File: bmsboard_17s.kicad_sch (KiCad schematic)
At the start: 0 parts

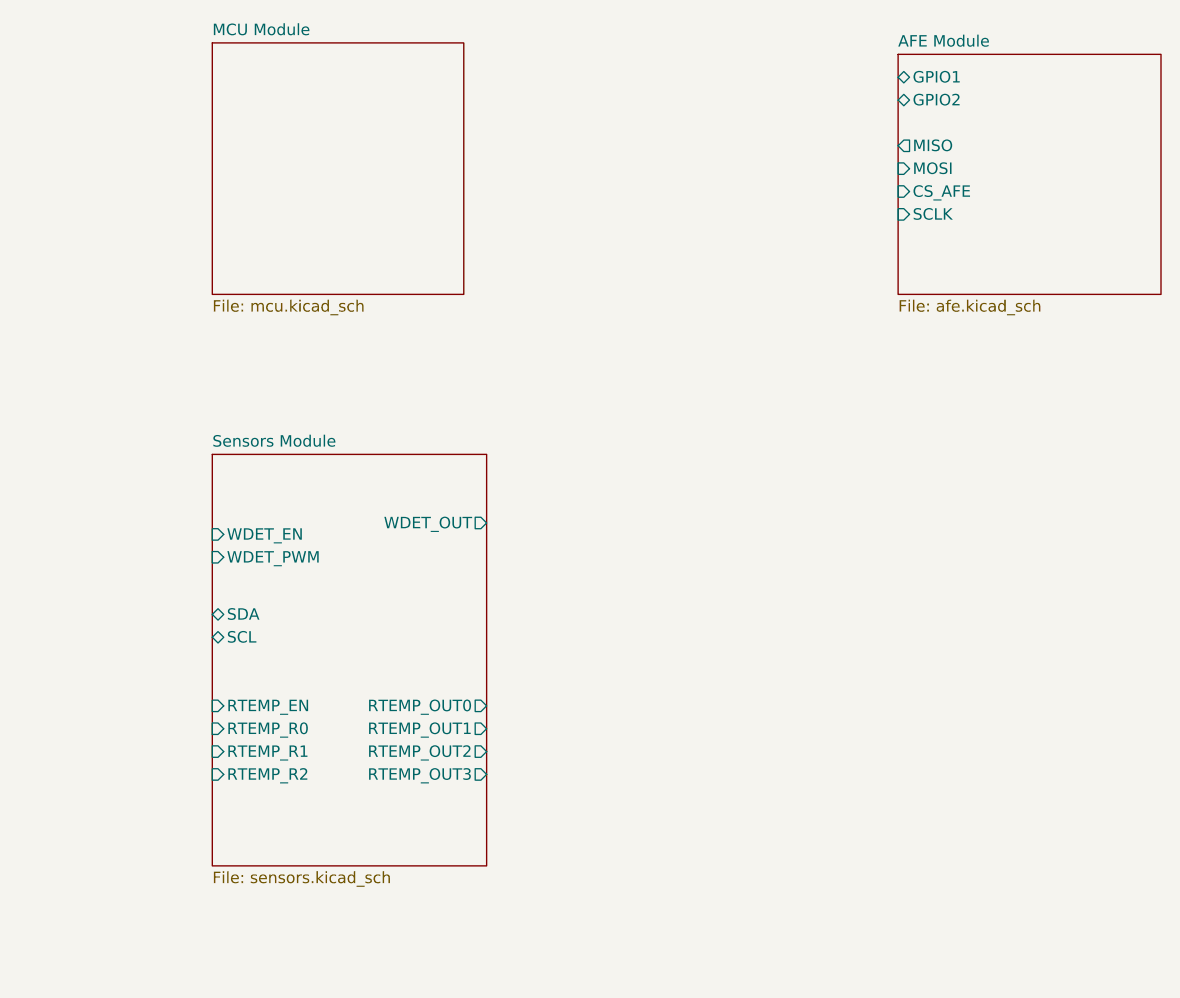
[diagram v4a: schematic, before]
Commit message: 分配MCU引脚，连接原理图，添加CAN收发器
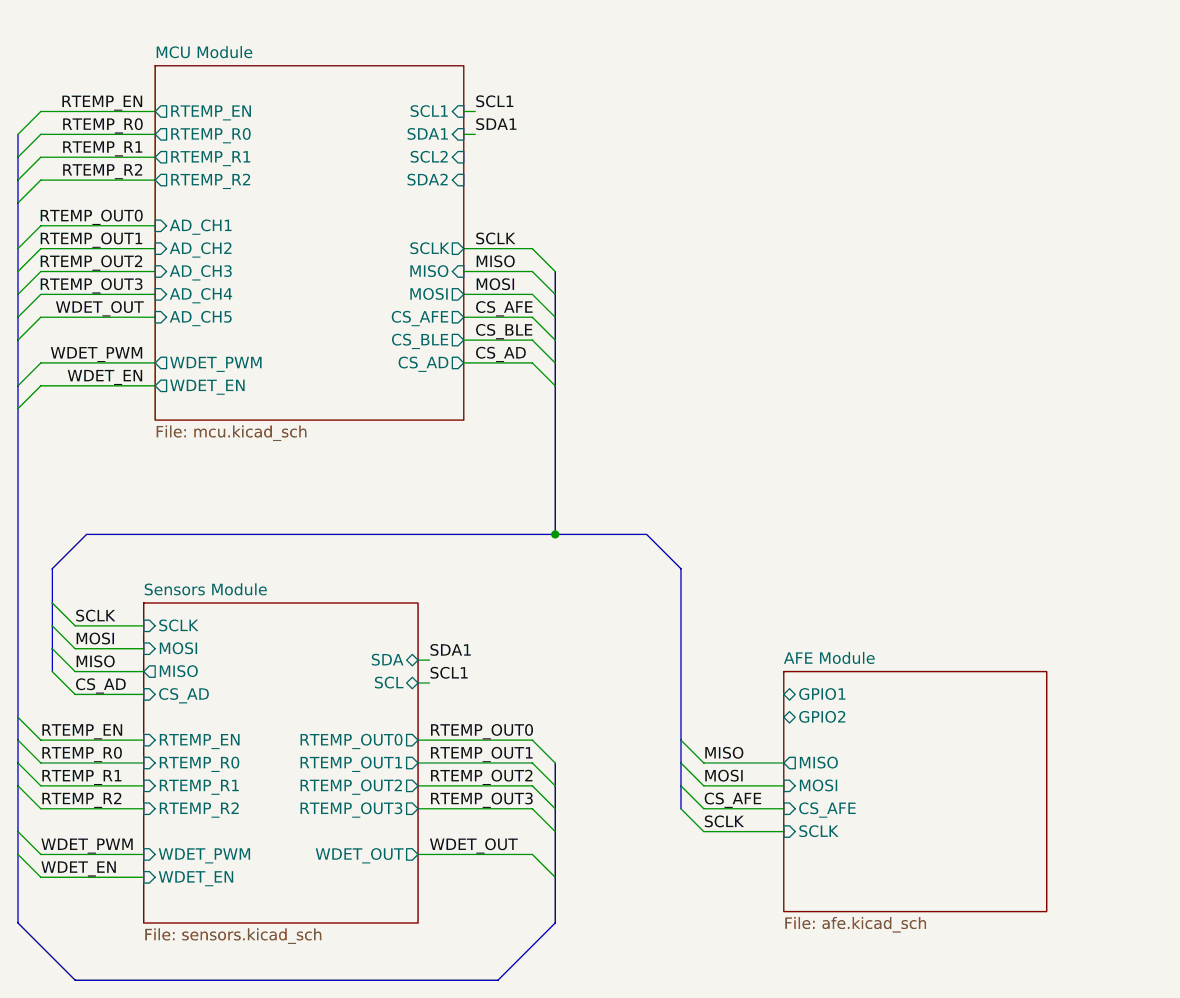
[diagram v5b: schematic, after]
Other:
- sheet MCU Module ports: added AD_CH1, AD_CH2, AD_CH3, AD_CH4, AD_CH5, CS_AD, CS_AFE, CS_BLE, MISO, MOSI, RTEMP_EN, RTEMP_R0, RTEMP_R1, RTEMP_R2, SCL1, SCL2, SCLK, SDA1, SDA2, WDET_EN, WDET_PWM; removed none
- sheet Sensors Module ports: added CS_AD, MISO, MOSI, SCLK; removed none

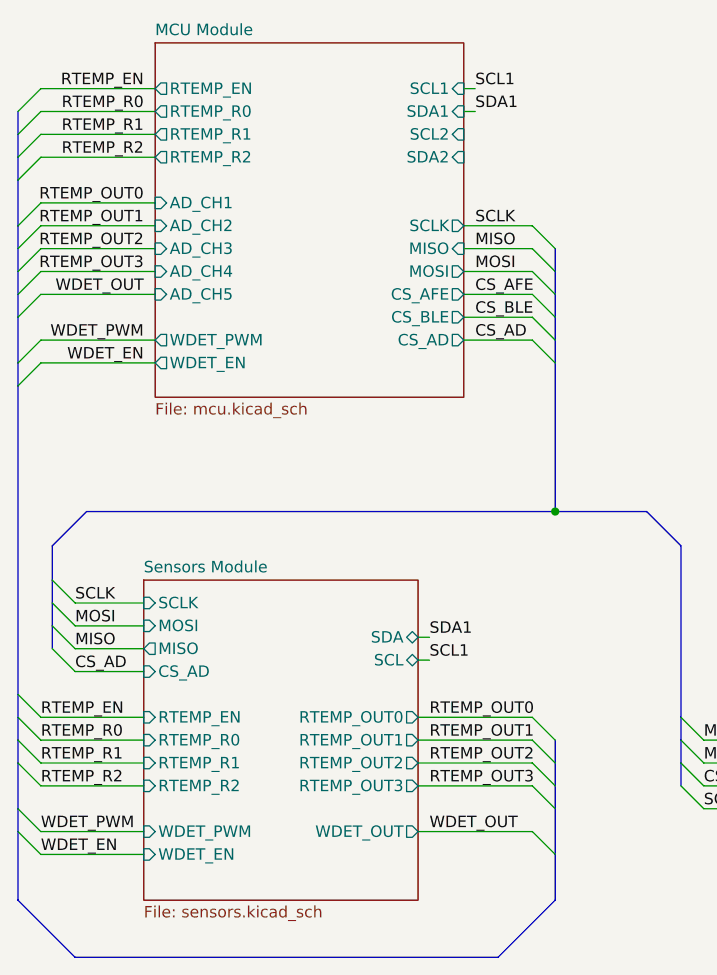
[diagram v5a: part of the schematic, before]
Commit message: 分配封装，添加RS485通信接口，调整布局，传感器连接到独立MCU上
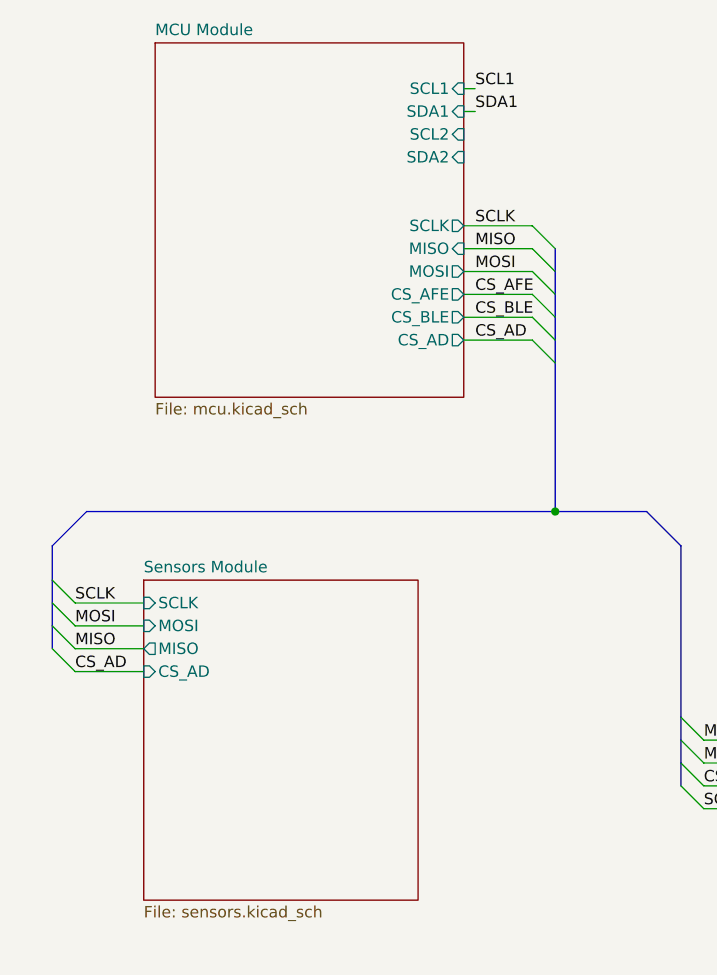
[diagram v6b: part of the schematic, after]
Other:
- sheet MCU Module ports: added none; removed AD_CH1, AD_CH2, AD_CH3, AD_CH4, AD_CH5, RTEMP_EN, RTEMP_R0, RTEMP_R1, RTEMP_R2, WDET_EN, WDET_PWM
- sheet Sensors Module ports: added none; removed RTEMP_EN, RTEMP_OUT0, RTEMP_OUT1, RTEMP_OUT2, RTEMP_OUT3, RTEMP_R0, RTEMP_R1, RTEMP_R2, SCL, SDA, WDET_EN, WDET_OUT, WDET_PWM

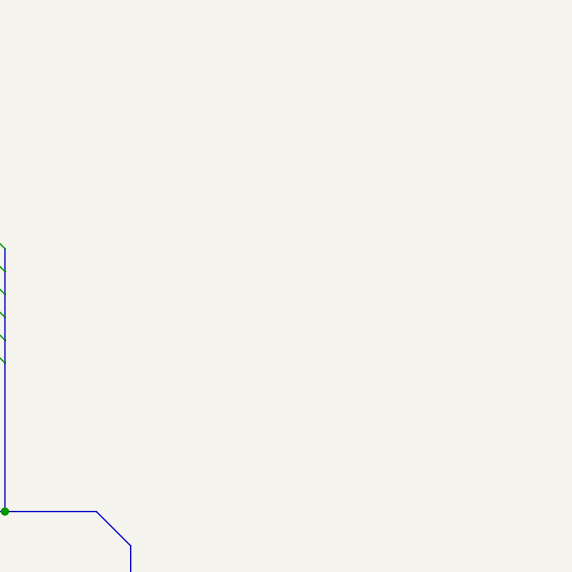
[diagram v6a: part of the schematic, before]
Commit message: 修改电源电路
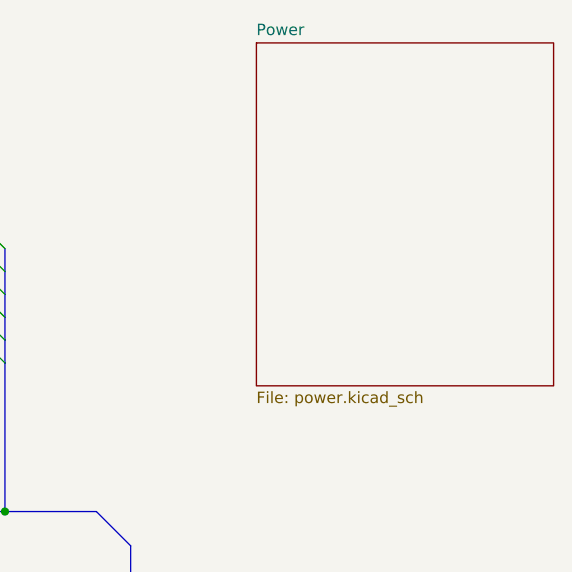
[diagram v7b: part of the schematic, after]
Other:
- added sheet Power (power.kicad_sch)
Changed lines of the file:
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@@
+		)
+	)
+	(sheet
+		(at 116.84 54.61)
+		(size 33.02 38.1)
+		(fields_autoplaced yes)
+		(stroke
+			(width 0.1524)
+			(type solid)
+		)
+		(fill
+			(color 0 0 0 0.0000)
+		)
+		(property "Sheetname" "Power"
+			(at 116.84 53.8984 0)
+			(effects
+				(font
+					(size 1.27 1.27)
+				)
+				(justify left bottom)
+			)
+		)
+		(property "Sheetfile" "power.kicad_sch"
+			(at 116.84 93.2946 0)
+			(effects
+				(font
+					(size 1.27 1.27)
+				)
+				(justify left top)
+			)
+		)
+		(instances
+			(project "bmsboard_17s"
+				(path "/8b3bc3d6-55f6-430e-b34e-509c7be416f4"
+					(page "5")
+				)
+			)
 		)
 	)
